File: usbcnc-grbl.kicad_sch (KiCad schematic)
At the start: 7 parts, among them J1 USB_B, J2 DB9_Female, J3 DB25_Female, U1 YAAJ_BluePill

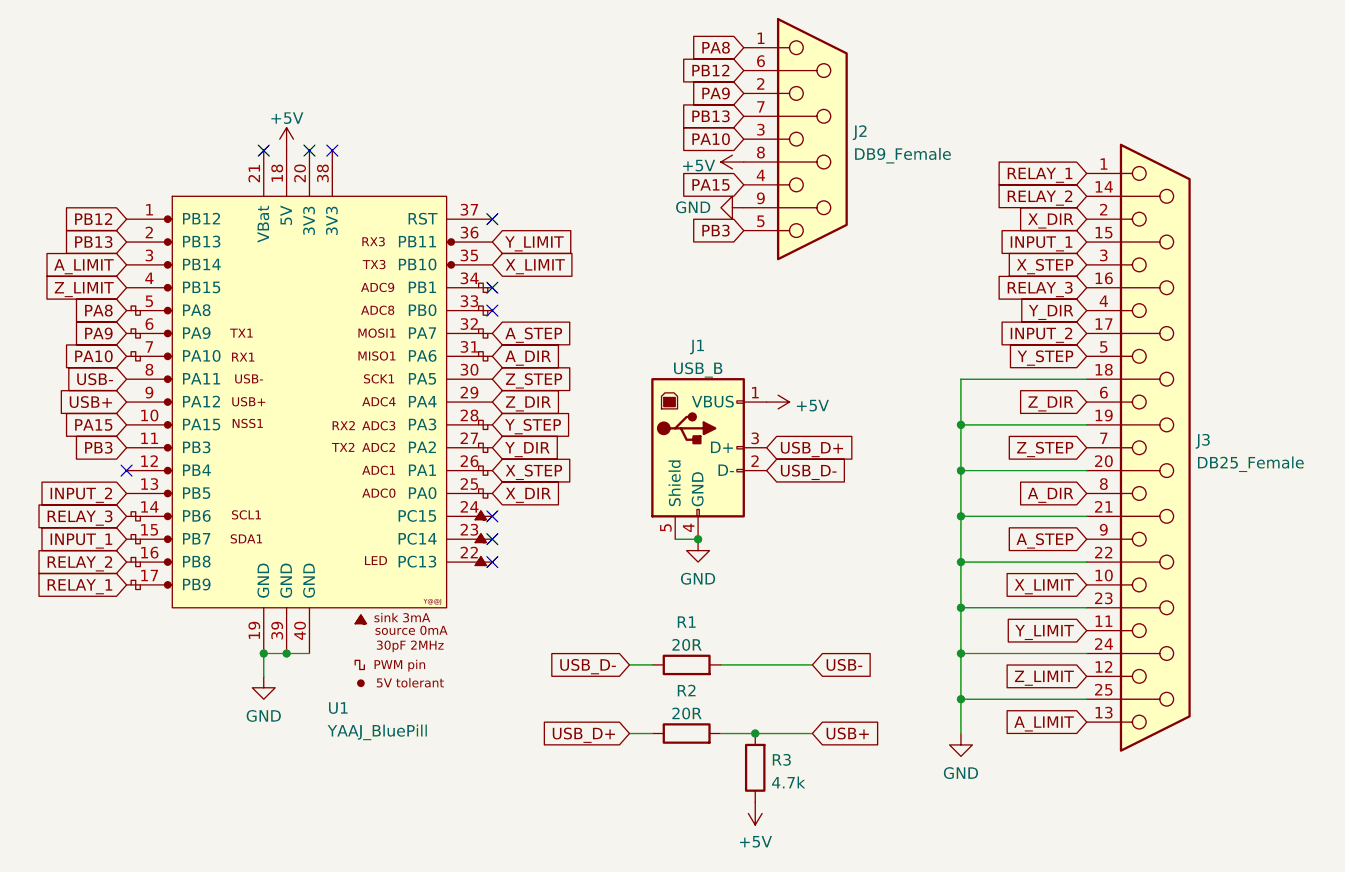
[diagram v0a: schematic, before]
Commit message: Fix pullup on USB
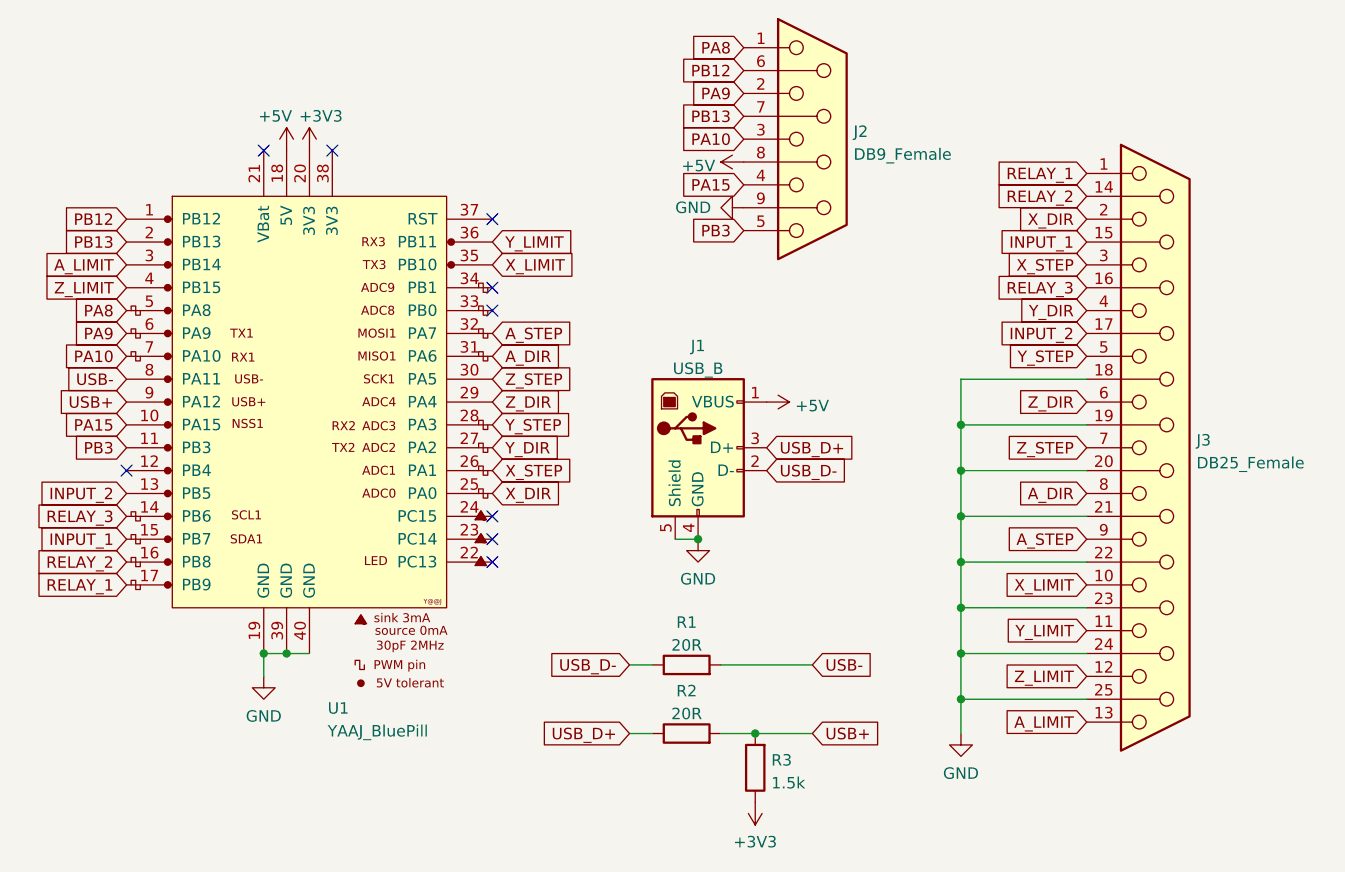
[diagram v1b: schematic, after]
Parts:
- R3: value 4.7k -> 1.5k
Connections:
- net +5V: no longer R3.1
- net +3V3: now reaches U1.20 (3V3)
- net +3V3: now also R3.1
- no-connect marks 10 -> 9
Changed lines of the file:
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@@
   (no_connect (at 115.57 63.5))
   (no_connect (at 123.19 63.5))
-  (no_connect (at 120.65 63.5))
   (wire (pts (xy 193.04 104.14) (xy 193.04 99.06))
     (stroke (width 0) (type default) (color 0 0 0 0))
@@
   )
   (symbol (lib_id "power:+5V") (at 118.11 63.5 0) (unit 1)
-    (in_bom yes) (on_board yes) (fields_autoplaced)
+    (in_bom yes) (on_board yes)
     (property "Reference" "#PWR02" (id 0) (at 118.11 67.31 0)
       (effects (font (size 1.27 1.27)) hide)
     )
-    (property "Value" "+5V" (id 1) (at 118.11 59.9242 0))
+    (property "Value" "+5V" (id 1) (at 116.84 59.69 0))
     (property "Footprint" "" (id 2) (at 118.11 63.5 0)
       (effects (font (size 1.27 1.27)) hide)
@@
       (effects (font (size 1.27 1.27)) (justify right))
     )
-    (property "Value" "4.7k" (id 1) (at 171.958 133.7822 0)
+    (property "Value" "1.5k" (id 1) (at 171.958 133.7822 0)
       (effects (font (size 1.27 1.27)) (justify right))
     )
@@
     (pin "2")
   )
+  (symbol (lib_id "power:+3V3") (at 120.65 63.5 0) (unit 1)
+    (in_bom yes) (on_board yes)
+    (property "Reference" "#PWR0101" (id 0) (at 120.65 67.31 0)
+      (effects (font (size 1.27 1.27)) hide)
+    )
+    (property "Value" "+3V3" (id 1) (at 121.92 59.69 0))
+    (property "Footprint" "" (id 2) (at 120.65 63.5 0)
+      (effects (font (size 1.27 1.27)) hide)
+    )
+    (property "Datasheet" "" (id 3) (at 120.65 63.5 0)
+      (effects (font (size 1.27 1.27)) hide)
+    )
+    (pin "1")
+  )
   (symbol (lib_id "power:+5V") (at 168.91 64.77 90) (unit 1)
     (in_bom yes) (on_board yes) (fields_autoplaced)
@@
     (pin "1")
   )
-  (symbol (lib_id "power:+5V") (at 170.18 135.89 180) (unit 1)
-    (in_bom yes) (on_board yes) (fields_autoplaced)
-    (property "Reference" "#PWR06" (id 0) (at 170.18 132.08 0)
-      (effects (font (size 1.27 1.27)) hide)
-    )
-    (property "Value" "+5V" (id 1) (at 170.18 140.3334 0))
+  (symbol (lib_id "power:+3V3") (at 170.18 135.89 180) (unit 1)
+    (in_bom yes) (on_board yes) (fields_autoplaced)
+    (property "Reference" "#PWR0102" (id 0) (at 170.18 132.08 0)
+      (effects (font (size 1.27 1.27)) hide)
+    )
+    (property "Value" "+3V3" (id 1) (at 170.18 140.3334 0))
     (property "Footprint" "" (id 2) (at 170.18 135.89 0)
       (effects (font (size 1.27 1.27)) hide)
@@
       (reference "#PWR05") (unit 1) (value "GND") (footprint "")
     )
-    (path "/a4f5fb0d-2531-460f-88a6-726eb9190225"
-      (reference "#PWR06") (unit 1) (value "+5V") (footprint "")
-    )
     (path "/dc1920ff-44d0-4b8d-b8a3-2f17ee0010d4"
       (reference "#PWR07") (unit 1) (value "+5V") (footprint "")
@@
       (reference "#PWR08") (unit 1) (value "GND") (footprint "")
     )
+    (path "/8314c204-404a-4ae8-bc90-65af4ca8bd6a"
+      (reference "#PWR0101") (unit 1) (value "+3V3") (footprint "")
+    )
+    (path "/a56a4fd1-de47-462e-86fb-3d3d7810caad"
+      (reference "#PWR0102") (unit 1) (value "+3V3") (footprint "")
+    )
     (path "/482328de-0f4b-4079-bedb-571c0f7fff8f"
       (reference "J1") (unit 1) (value "USB_B") (footprint "Connector_USB:USB_B_OST_USB-B1HSxx_Horizontal")
@@
     )
     (path "/80947b65-18ce-4ad2-b610-2573de8c6b20"
-      (reference "R3") (unit 1) (value "4.7k") (footprint "Resistor_SMD:R_0805_2012Metric_Pad1.20x1.40mm_HandSolder")
+      (reference "R3") (unit 1) (value "1.5k") (footprint "Resistor_SMD:R_0805_2012Metric_Pad1.20x1.40mm_HandSolder")
     )
     (path "/cc718e8f-7b44-4407-9bd2-f4db5b7464b1"
